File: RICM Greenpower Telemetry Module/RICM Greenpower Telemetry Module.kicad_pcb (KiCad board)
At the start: 2 copper layers, 35 parts, among them J1 Conn_01x02_Female, J10 Conn_01x02_Female, J11 Conn_01x02_Female, J2 Conn_01x02_Female, J3 Conn_01x02_Female, J4 Jack-DC, J5 Conn_01x05_Female, J6 Conn_02x04_Counter_Clockwise, J7 Conn_01x03_Female, J8 Conn_01x03_Female, J9 Conn_01x04_Female, U1 Pico, U2 MPU_6050_module, U3 Adafruit_MicroSD_SPI_SDIO, U4 LTC2990

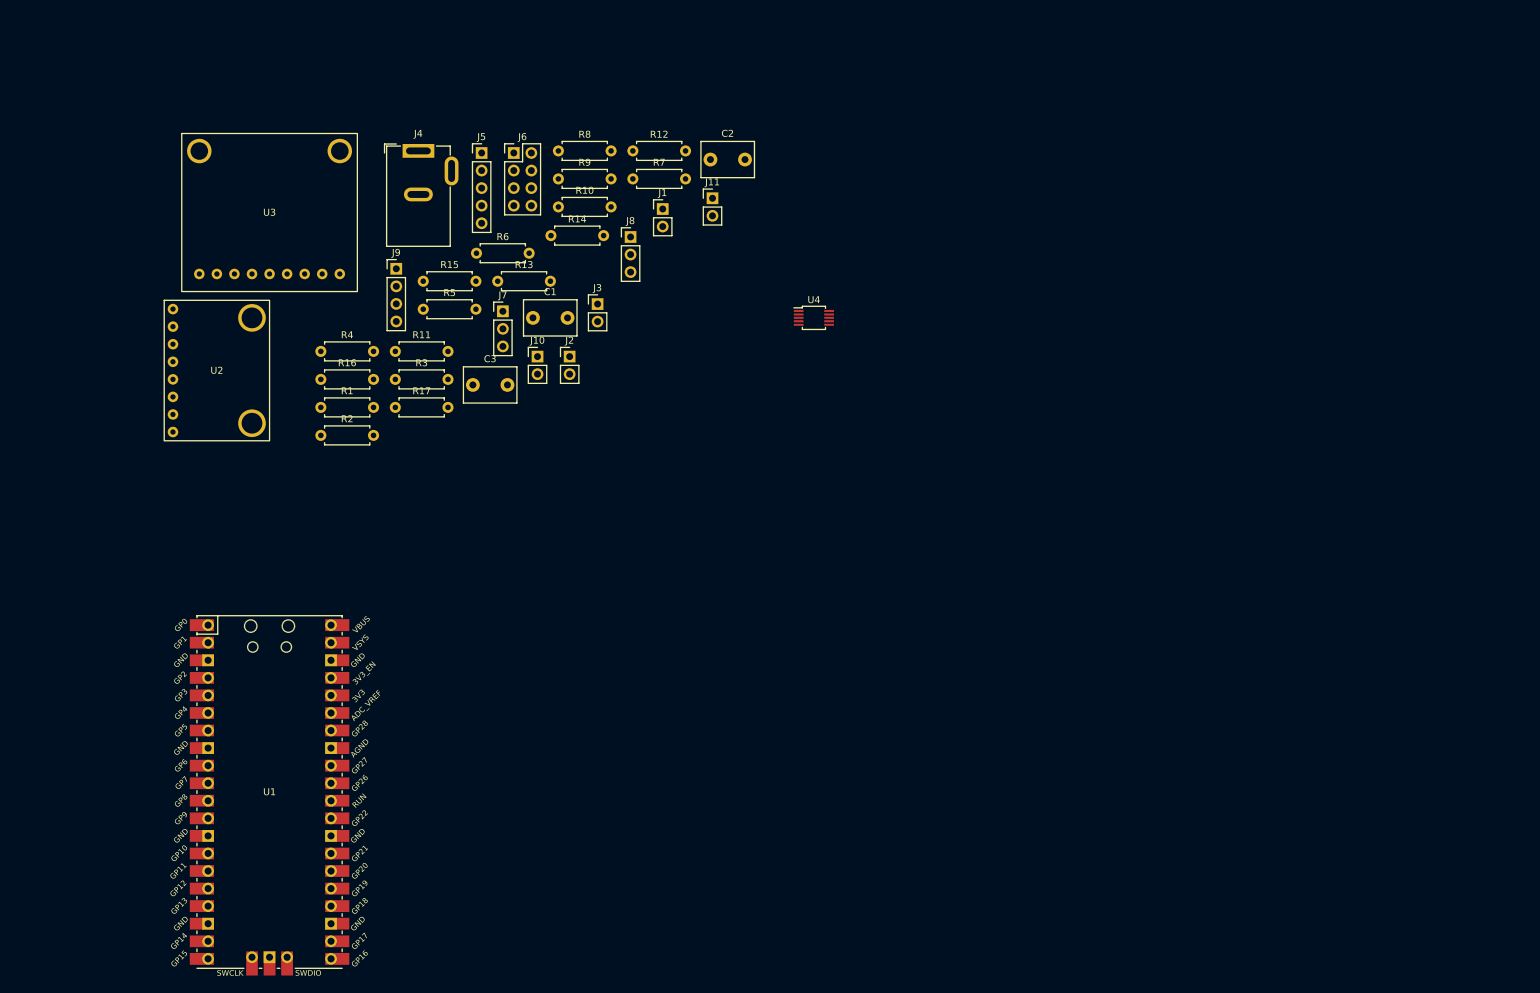
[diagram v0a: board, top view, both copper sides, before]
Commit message: bug fixes and missing connections
Fixed the short from the first battery voltage to ground
Added a chip select for interfacing the SD card over SPI
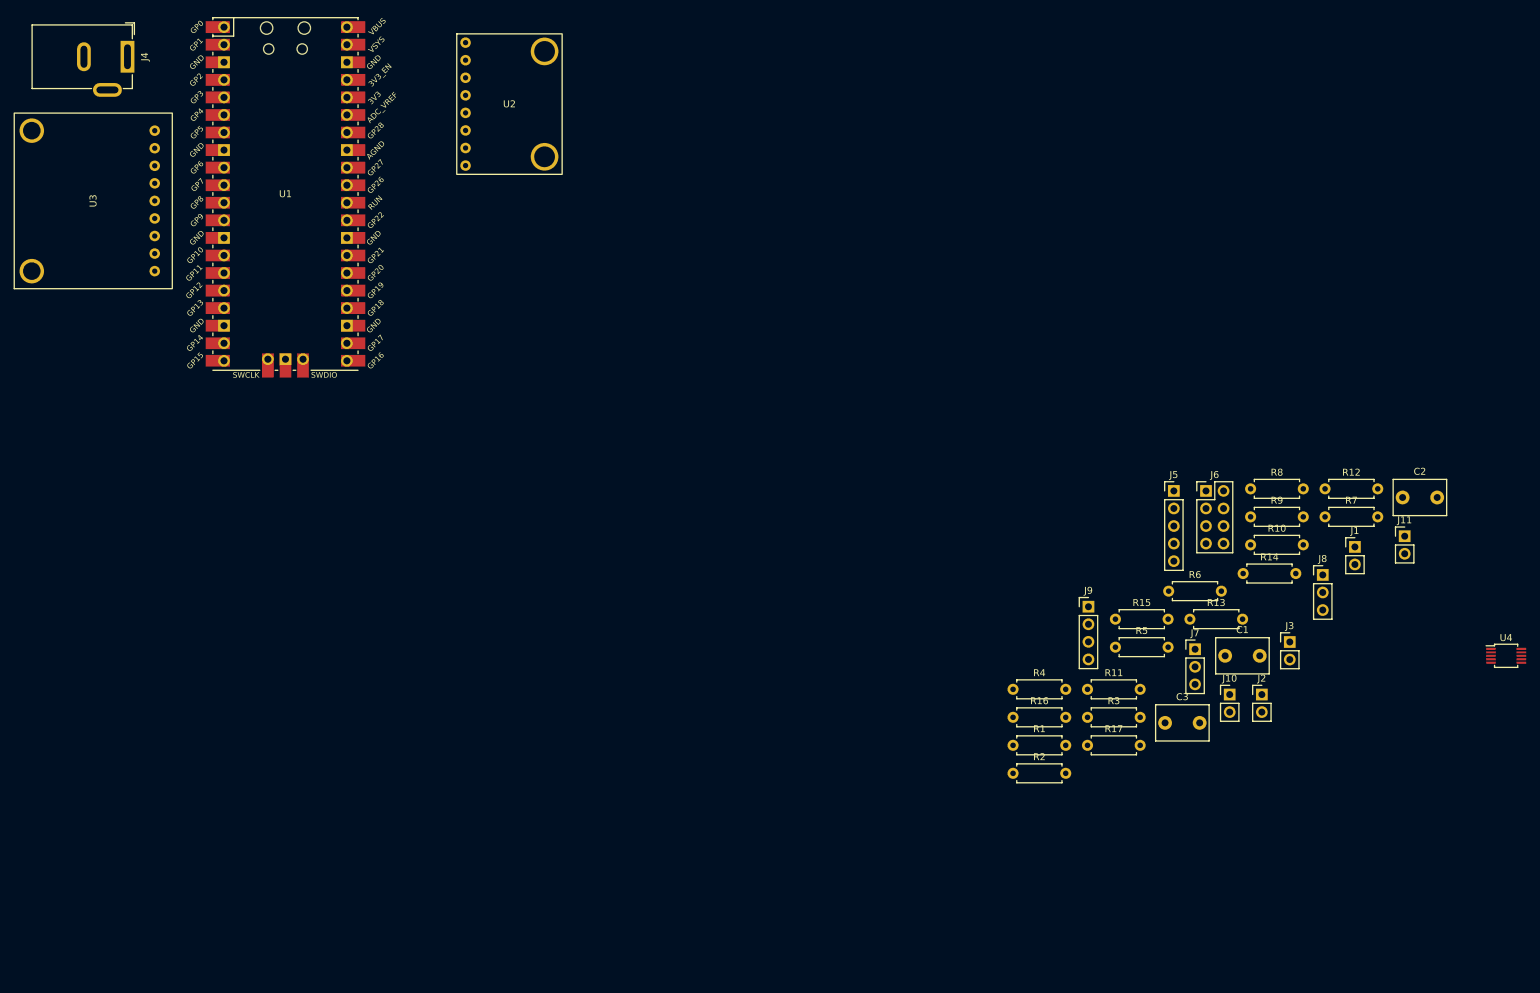
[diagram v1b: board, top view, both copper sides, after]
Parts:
- moved C2 111.4 mm to (202.0, 71.7)
- moved J1 111.4 mm to (195.1, 78.8)
- moved J5 111.4 mm to (168.9, 70.8)
- moved J6 111.4 mm to (173.6, 70.8)
- moved J7 111.4 mm to (172.0, 93.7)
- moved J8 111.4 mm to (190.4, 82.9)
- moved J9 111.4 mm to (156.6, 87.5)
- moved R10 111.4 mm to (180.0, 78.5)
- moved R11 111.4 mm to (156.4, 99.5)
- moved R12 111.4 mm to (190.8, 70.5)
- moved R13 111.4 mm to (171.2, 89.3)
- moved R17 111.4 mm to (156.4, 107.5)
- moved R3 111.4 mm to (156.4, 103.5)
- moved R6 111.4 mm to (168.2, 85.2)
- moved R7 111.4 mm to (190.8, 74.5)
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
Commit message: first draft of layout
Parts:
- removed J11: Conn_01x02_Female, Connector_PinHeader_2.54mm:PinHeader_1x02_P2.54mm_Vertical
- C1, C2, C3: footprint Capacitor_THT:C_Disc_D7.5mm_W5.0mm_P5.00mm -> Capacitor_THT:C_Disc_D4.7mm_W2.5mm_P5.00mm
- J10: footprint Connector_PinHeader_2.54mm:PinHeader_1x02_P2.54mm_Vertical -> Connector_PinHeader_2.54mm:PinHeader_1x03_P2.54mm_Vertical
- R16: value 30k -> 68k
- moved J1 174.1 mm to (24.1, 111.8), turned to 180 degrees
- moved J8 173.4 mm to (17.0, 85.1), turned to 90 degrees
- moved J3 169.0 mm to (17.8, 111.8), turned to 180 degrees
- moved U4 163.7 mm to (53.3, 90.2)
- moved R7 160.6 mm to (31.0, 58.4)
- moved J6 156.8 mm to (17.0, 60.9), turned to 90 degrees
- moved R14 156.3 mm to (22.9, 91.4), turned to 180 degrees
- moved J7 155.8 mm to (17.0, 77.5), turned to 90 degrees
- moved C2 153.0 mm to (50.8, 95.2)
- moved R9 152.4 mm to (27.9, 85.1)
- moved R8 152.2 mm to (27.9, 77.5)
- moved J5 151.9 mm to (17.0, 69.8), turned to 90 degrees
- moved J2 151.6 mm to (30.5, 111.8), turned to 180 degrees
- moved R12 144.0 mm to (51.4, 106.7), turned to 90 degrees
- moved R6 139.1 mm to (31.0, 62.2)
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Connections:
- J6 pad 3: I2C_SDA -> I2C0_SDA
- J6 pad 4: I2C_SCL -> I2C0_SCL
- R16 pad 1: Net-(J11-Pad2) -> Net-(J10-Pad3)
- U1 pad 17: unconnected-(U1-Pad17) -> SD_CS
- U1 pad 19: I2C_SDA -> I2C0_SDA
- U1 pad 20: I2C_SCL -> I2C0_SCL
- U1 pad 21: unconnected-(U1-Pad21) -> I2C_SDA
- U1 pad 22: unconnected-(U1-Pad22) -> I2C_SCL
- U3 pad 6: unconnected-(U3-Pad6) -> SD_CS
- U4 pad 6: I2C_SCL -> I2C_SDA
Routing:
- net GND: track 0.00 -> 354.9 mm
- net +5V: track 0.00 -> 202.3 mm, vias 0 -> 1
- net +3V3: track 0.00 -> 189.4 mm
- net AGND: track 0.00 -> 132.4 mm
- net THERM_0: track 0.00 -> 132.2 mm
- net THERM_2: track 0.00 -> 132.1 mm
- net THERM_1: track 0.00 -> 128.8 mm
- net Net-(J10-Pad2): track 0.00 -> 85.1 mm
- net SPD_1: track 0.00 -> 64.0 mm
- net Net-(J6-Pad5): track 0.00 -> 54.7 mm
- net Net-(J6-Pad6): track 0.00 -> 52.2 mm
- net Net-(J6-Pad7): track 0.00 -> 47.1 mm, vias 0 -> 1
- net Net-(J6-Pad8): track 0.00 -> 46.7 mm, vias 0 -> 1
- net ACC_INT: track 0.00 -> 44.7 mm, vias 0 -> 1
- net Net-(C3-Pad1): track 0.00 -> 43.2 mm, vias 0 -> 2
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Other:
- board outline added: 57.1 x 104.1 mm
- board text added: "+5V"
- board text added: "BATT_V"
- board text added: "CURR_SENS"
- board text added: "DISPLAY"
- board text added: "MISC_IO"
- board text added: "SPD_0"
- board text added: "SPD_1"
- board text added: "THERM_0"
- board text added: "THERM_1"
- board text added: "THERM_2"

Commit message: Polyfuse and missing connections
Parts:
- added F1: Polyfuse, Capacitor_THT:C_Disc_D5.0mm_W2.5mm_P5.00mm, F.Cu at (34.3, 19.1)
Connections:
- J4 pad 1: +5V -> Net-(J4-Pad1)
- J4 pad 3: (no net) -> GND
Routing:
- net SPD_0: track 37.7 -> 58.6 mm
- net GND: track 354.9 -> 371.7 mm
- net Net-(J4-Pad1): track 0.00 -> 5.24 mm
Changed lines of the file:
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@@
   (net 52 "unconnected-(U3-Pad7)")
   (net 53 "unconnected-(U3-Pad8)")
+  (net 54 "Net-(J4-Pad1)")
   (footprint "Connector_PinHeader_2.54mm:PinHeader_1x03_P2.54mm_Vertical" (layer "F.Cu")
     (at 17.025 77.48 90)
@@
     )
   )
+  (footprint "Capacitor_THT:C_Disc_D5.0mm_W2.5mm_P5.00mm" (layer "F.Cu")
+    (at 34.33 19.05)
+    (descr "C, Disc series, Radial, pin pitch=5.00mm, , diameter*width=5*2.5mm^2, Capacitor, http://cdn-reichelt.de/documents/datenblatt/B300/DS_KERKO_TC.pdf")
+    (tags "C Disc series Radial pin pitch 5.00mm  diameter 5mm width 2.5mm Capacitor")
+    (property "Sheetfile" "RICM Greenpower Telemetry Module.kicad_sch")
+    (property "Sheetname" "")
+    (attr through_hole)
+    (fp_text reference "F1" (at 2.5 -2.5) (layer "F.SilkS")
+      (effects (font (size 1 1) (thickness 0.15)))
+    )
+    (fp_text value "Polyfuse" (at 2.5 2.5) (layer "F.Fab")
+      (effects (font (size 1 1) (thickness 0.15)))
+    )
+    (fp_text user "${REFERENCE}" (at 2.5 0) (layer "F.Fab")
+      (effects (font (size 1 1) (thickness 0.15)))
+    )
+    (fp_line (start -0.12 -1.37) (end -0.12 -1.055) (layer "F.SilkS") (width 0.12))
+    (fp_line (start 5.12 -1.37) (end 5.12 -1.055) (layer "F.SilkS") (width 0.12))
+    (fp_line (start 5.12 1.055) (end 5.12 1.37) (layer "F.SilkS") (width 0.12))
+    (fp_line (start -0.12 1.055) (end -0.12 1.37) (layer "F.SilkS") (width 0.12))
+    (fp_line (start -0.12 1.37) (end 5.12 1.37) (layer "F.SilkS") (width 0.12))
+    (fp_line (start -0.12 -1.37) (end 5.12 -1.37) (layer "F.SilkS") (width 0.12))
+    (fp_line (start -1.05 1.5) (end 6.05 1.5) (layer "F.CrtYd") (width 0.05))
+    (fp_line (start 6.05 1.5) (end 6.05 -1.5) (layer "F.CrtYd") (width 0.05))
+    (fp_line (start 6.05 -1.5) (end -1.05 -1.5) (layer "F.CrtYd") (width 0.05))
+    (fp_line (start -1.05 -1.5) (end -1.05 1.5) (layer "F.CrtYd") (width 0.05))
+    (fp_line (start 0 1.25) (end 5 1.25) (layer "F.Fab") (width 0.1))
+    (fp_line (start 5 1.25) (end 5 -1.25) (layer "F.Fab") (width 0.1))
+    (fp_line (start 5 -1.25) (end 0 -1.25) (layer "F.Fab") (width 0.1))
+    (fp_line (start 0 -1.25) (end 0 1.25) (layer "F.Fab") (width 0.1))
+    (pad "1" thru_hole circle (at 0 0) (size 1.6 1.6) (drill 0.8) (layers *.Cu *.Mask)
+      (net 54 "Net-(J4-Pad1)") (pintype "passive"))
+    (pad "2" thru_hole circle (at 5 0) (size 1.6 1.6) (drill 0.8) (layers *.Cu *.Mask)
+      (net 6 "+5V") (pintype "passive"))
+    (model "${KICAD6_3DMODEL_DIR}/Capacitor_THT.3dshapes/C_Disc_D5.0mm_W2.5mm_P5.00mm.wrl"
+      (offset (xyz 0 0 0))
+      (scale (xyz 1 1 1))
+      (rotate (xyz 0 0 0))
+    )
+  )
   (footprint "Connector_BarrelJack:BarrelJack_GCT_DCJ200-10-A_Horizontal" (layer "F.Cu")
     (at 29.21 19.67 -90)
@@
     (fp_line (start -4.5 0.4) (end -3.5 -0.6) (layer "F.Fab") (width 0.1))
     (pad "1" thru_hole rect (at 0 0 270) (size 4.6 2) (drill oval 3.6 1) (layers *.Cu *.Mask)
-      (net 6 "+5V") (pintype "passive"))
+      (net 54 "Net-(J4-Pad1)") (pintype "passive"))
     (pad "2" thru_hole oval (at 0 6.3 270) (size 4.2 2) (drill oval 3.2 1) (layers *.Cu *.Mask)
       (net 4 "GND") (pintype "passive"))
-    (pad "3" thru_hole oval (at 4.8 2.9 270) (size 2 4.2) (drill oval 1 3.2) (layers *.Cu *.Mask))
+    (pad "3" thru_hole oval (at 4.8 2.9 270) (size 2 4.2) (drill oval 1 3.2) (layers *.Cu *.Mask)
+      (net 4 "GND"))
     (model "${KICAD6_3DMODEL_DIR}/Connector_BarrelJack.3dshapes/BarrelJack_GCT_DCJ200-10-A_Horizontal.wrl"
       (offset (xyz 0 0 0))
@@
     )
     (fp_text user "ADC_VREF" (at 14 -12.5 45) (layer "F.SilkS")
-      (effects (font (size 0.8 0.8) (thickness 0.15)))
+      (effects (font (size 0.8 0.6) (thickness 0.15)))
     )
     (fp_text user "GP12" (at -13.2 13.97 45) (layer "F.SilkS")
@@
   )
   (gr_rect (start 12.7 12.7) (end 69.85 116.84) (layer "Edge.Cuts") (width 0.1) (fill none))
-  (gr_text "+5V" (at 34.29 19.812 90) (layer "F.SilkS")
+  (gr_text "+5V" (at 35.6 22.86) (layer "F.SilkS")
     (effects (font (size 3 3) (thickness 0.3)))
   )
@@
   (segment (start 22.91 19.67) (end 22.91 21.07) (width 1.5) (layer "F.Cu") (net 4))
   (segment (start 68.58 22.19) (end 68.58 46.99) (width 0.5) (layer "F.Cu") (net 4))
+  (segment (start 46.02 21.89) (end 48.26 24.13) (width 0.5) (layer "F.Cu") (net 4))
   (segment (start 52.748489 91.269511) (end 51.14 91.269511) (width 0.5) (layer "F.Cu") (net 4))
   (segment (start 68.58 46.99) (end 68.58 59.69) (width 0.5) (layer "F.Cu") (net 4))
   (segment (start 54.102 89.916) (end 52.748489 91.269511) (width 0.5) (layer "F.Cu") (net 4))
+  (segment (start 46.69 34.59) (end 48.26 33.02) (width 0.5) (layer "F.Cu") (net 4))
+  (segment (start 48.26 33.02) (end 48.26 24.13) (width 0.5) (layer "F.Cu") (net 4))
   (segment (start 26.31 24.47) (end 29.609022 24.47) (width 1.5) (layer "F.Cu") (net 4))
   (segment (start 68.28 21.89) (end 68.58 22.19) (width 0.5) (layer "F.Cu") (net 4))
@@
   (segment (start 62.85 21.89) (end 68.28 21.89) (width 0.5) (layer "F.Cu") (net 4))
   (segment (start 45.07 21.89) (end 32.189022 21.89) (width 1.5) (layer "F.Cu") (net 4))
+  (segment (start 45.07 21.89) (end 46.02 21.89) (width 0.5) (layer "F.Cu") (net 4))
+  (segment (start 45.07 34.59) (end 46.69 34.59) (width 0.5) (layer "F.Cu") (net 4))
   (segment (start 68.28 47.29) (end 62.85 47.29) (width 0.5) (layer "F.Cu") (net 4))
   (segment (start 62.85 21.89) (end 45.07 21.89) (width 0.5) (layer "F.Cu") (net 4))
@@
   (segment (start 20.32 24.13) (end 19.05 25.4) (width 0.5) (layer "F.Cu") (net 6))
   (segment (start 26.05 16.51) (end 21.59 16.51) (width 0.5) (layer "F.Cu") (net 6))
-  (segment (start 31.13 19.67) (end 33.02 17.78) (width 1.5) (layer "F.Cu") (net 6))
-  (segment (start 33.02 13.97) (end 67.31 13.97) (width 1.5) (layer "F.Cu") (net 6))
+  (segment (start 26.05 16.51) (end 36.83 16.51) (width 0.5) (layer "F.Cu") (net 6))
   (segment (start 16.495 60.945) (end 17.03 60.945) (width 0.5) (layer "F.Cu") (net 6))
   (segment (start 22.105 75.445) (end 21.59 74.93) (width 0.5) (layer "F.Cu") (net 6))
@@
   (segment (start 20.32 17.78) (end 20.32 24.13) (width 0.5) (layer "F.Cu") (net 6))
   (segment (start 19.05 25.4) (end 15.24 25.4) (width 0.5) (layer "F.Cu") (net 6))
+  (segment (start 39.33 14.01) (end 39.37 13.97) (width 1.5) (layer "F.Cu") (net 6))
   (segment (start 55.54 89.17) (end 54.245 89.17) (width 0.25) (layer "F.Cu") (net 6))
   (segment (start 13.97 26.67) (end 13.97 58.42) (width 0.5) (layer "F.Cu") (net 6))
+  (segment (start 39.37 13.97) (end 67.31 13.97) (width 1.5) (layer "F.Cu") (net 6))
   (segment (start 13.97 58.42) (end 16.495 60.945) (width 0.5) (layer "F.Cu") (net 6))
   (segment (start 67.31 13.97) (end 67.31 19.05) (width 1.5) (layer "F.Cu") (net 6))
   (segment (start 21.59 74.93) (end 16.51 74.93) (width 0.5) (layer "F.Cu") (net 6))
   (segment (start 67.31 19.05) (end 67.01 19.35) (width 1.5) (layer "F.Cu") (net 6))
+  (segment (start 36.83 16.51) (end 39.37 19.05) (width 0.5) (layer "F.Cu") (net 6))
   (segment (start 57.785 88.9) (end 63.5 88.9) (width 0.25) (layer "F.Cu") (net 6))
-  (segment (start 29.21 19.67) (end 31.13 19.67) (width 1.5) (layer "F.Cu") (net 6))
   (segment (start 13.97 72.39) (end 16.51 74.93) (width 0.5) (layer "F.Cu") (net 6))
   (segment (start 45.72 86.995) (end 52.07 86.995) (width 0.25) (layer "F.Cu") (net 6))
   (segment (start 55.54 89.17) (end 57.515 89.17) (width 0.25) (layer "F.Cu") (net 6))
+  (segment (start 39.33 19.05) (end 39.33 14.01) (width 1.5) (layer "F.Cu") (net 6))
   (segment (start 13.97 72.39) (end 13.97 58.42) (width 0.5) (layer "F.Cu") (net 6))
   (segment (start 22.105 77.48) (end 22.105 75.445) (width 0.5) (layer "F.Cu") (net 6))
   (segment (start 57.515 89.17) (end 57.785 88.9) (width 0.25) (layer "F.Cu") (net 6))
-  (segment (start 33.02 17.78) (end 33.02 13.97) (width 1.5) (layer "F.Cu") (net 6))
-  (segment (start 29.21 19.67) (end 26.05 16.51) (width 0.5) (layer "F.Cu") (net 6))
   (via (at 45.72 86.995) (size 0.8) (drill 0.4) (layers "F.Cu" "B.Cu") (net 6))
   (segment (start 31.76 85.1) (end 27.94 85.1) (width 0.5) (layer "B.Cu") (net 6))
@@
   (segment (start 33.782 28.448) (end 37.8 24.43) (width 0.25) (layer "B.Cu") (net 21))
   (segment (start 37.8 24.43) (end 45.07 24.43) (width 0.25) (layer "B.Cu") (net 21))
+  (segment (start 17.025 77.48) (end 17.025 77.985) (width 0.25) (layer "F.Cu") (net 22))
   (segment (start 47.625 65.415) (end 47.625 65.405) (width 0.25) (layer "F.Cu") (net 22))
+  (segment (start 33.02 80.01) (end 35.56 77.47) (width 0.25) (layer "F.Cu") (net 22))
+  (segment (start 17.025 77.985) (end 19.05 80.01) (width 0.25) (layer "F.Cu") (net 22))
   (segment (start 35.56 77.48) (end 47.625 65.415) (width 0.25) (layer "F.Cu") (net 22))
+  (segment (start 19.05 80.01) (end 33.02 80.01) (width 0.25) (layer "F.Cu") (net 22))
   (segment (start 60.66 52.37) (end 62.85 52.37) (width 0.25) (layer "F.Cu") (net 22))
   (segment (start 47.625 65.405) (end 60.66 52.37) (width 0.25) (layer "F.Cu") (net 22))
@@
   (segment (start 38.1 48.514) (end 36.576 46.99) (width 0.25) (layer "B.Cu") (net 51))
   (segment (start 38.1 53.594) (end 38.1 48.514) (width 0.25) (layer "B.Cu") (net 51))
+  (segment (start 31.6 19.8) (end 29.4 19.8) (width 1.5) (layer "F.Cu") (net 54))
+  (segment (start 34.33 19.05) (end 32.35 19.05) (width 1.5) (layer "F.Cu") (net 54))
+  (segment (start 32.35 19.05) (end 31.6 19.8) (width 1.5) (layer "F.Cu") (net 54))
 )
